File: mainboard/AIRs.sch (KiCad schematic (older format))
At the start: 37 parts, among them J10 AIR+, J6 AIR-, K1 KT12-1A, Q3 DMN10H220L, Q5 2N7002NXAKR, Q6 2N7002NXAKR, Q7 DMN10H220L, U11 TS3704IPT

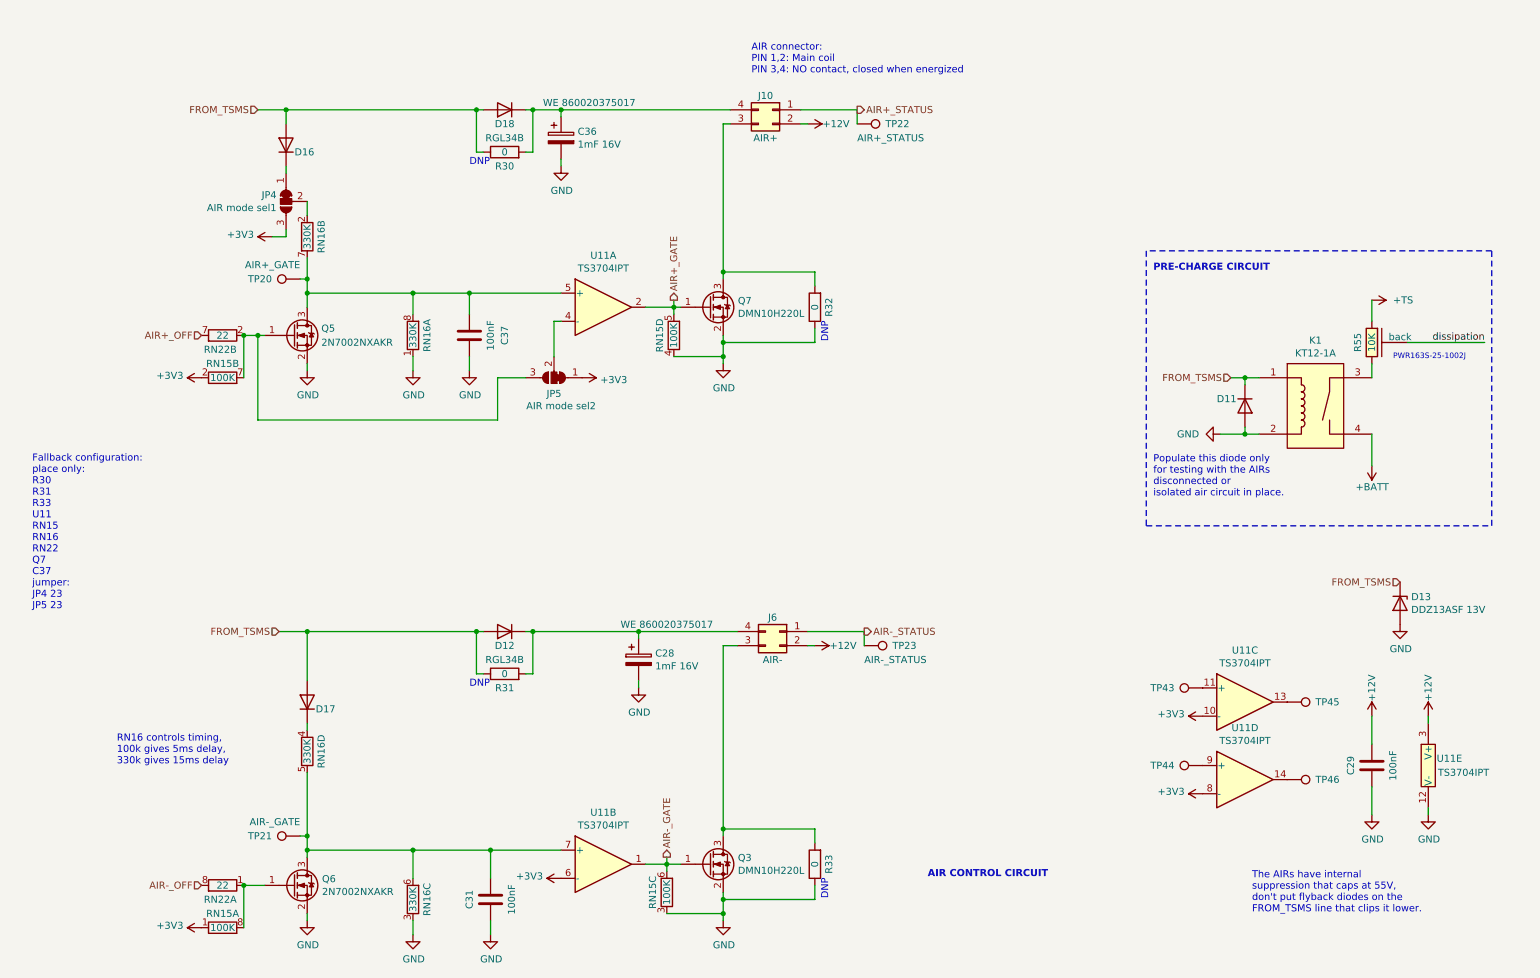
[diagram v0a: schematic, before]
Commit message: Renamed handcart detection
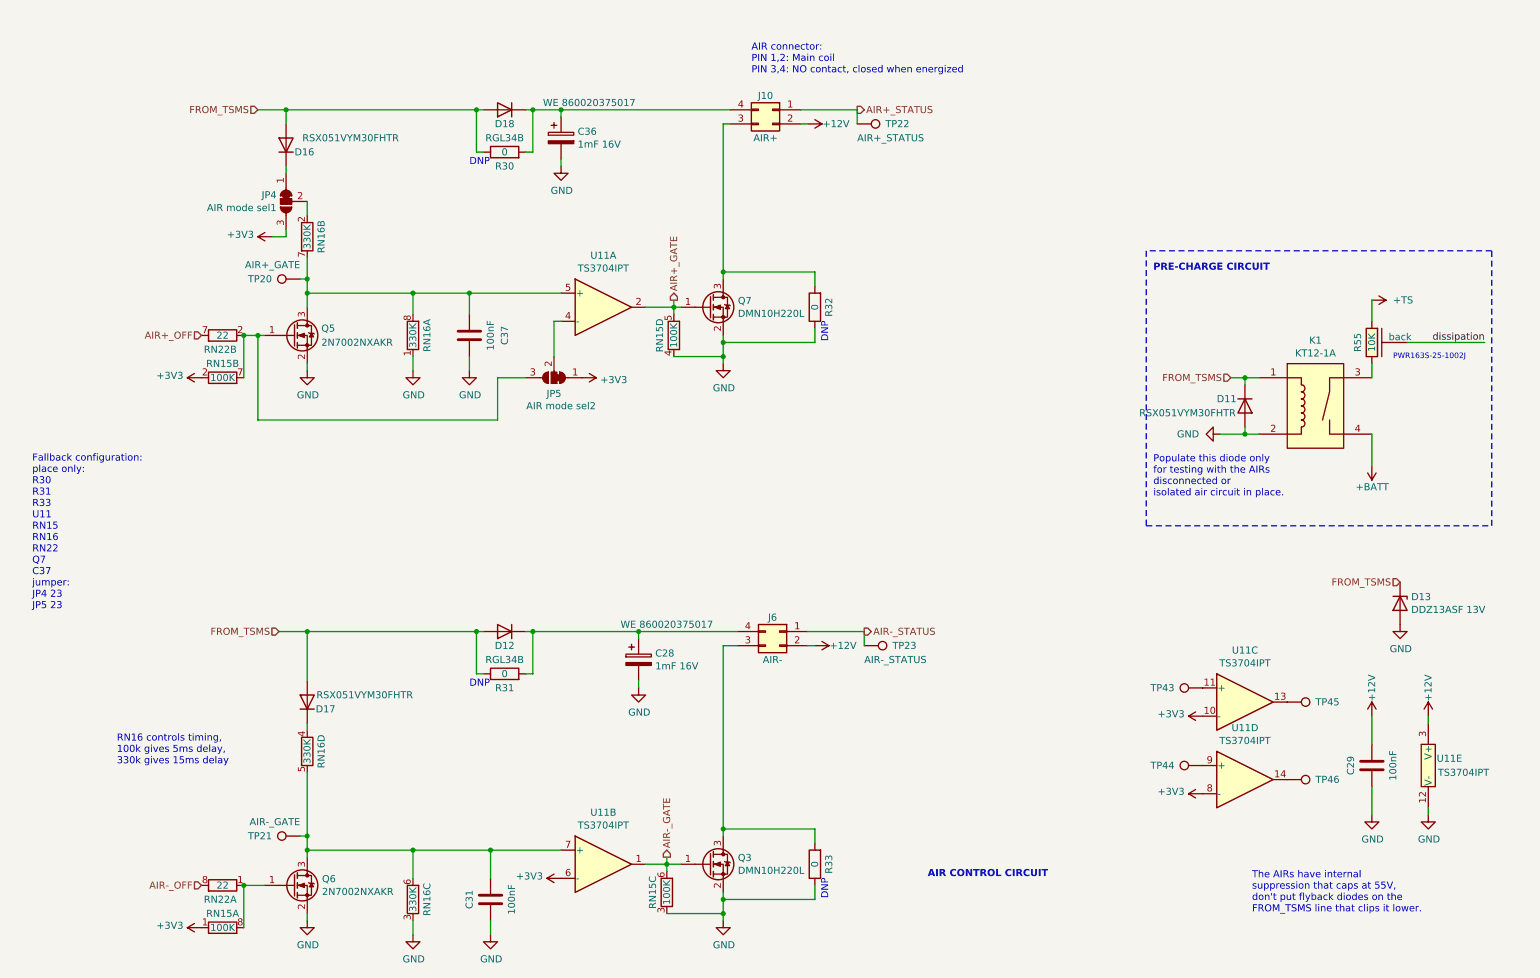
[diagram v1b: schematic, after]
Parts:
- D11, D16, D17: value D -> RSX051VYM30FHTR
- Q5, Q6: value 2N7002NXAKR -> 2N7002NXAKR
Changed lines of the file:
@@
 AR Path="/60A98674/60AA9B96" Ref="D16"  Part="1"
 F 0 "D16" V 2400 1250 50  0000 L CNN
-F 1 "D" V 2500 1250 50  0001 L CNN
+F 1 "RSX051VYM30FHTR" V 2500 650 50  0000 L CNN
 F 2 "MainBoard:SOD_323HE" H 2450 1450 50  0001 C CNN
 F 3 "~" H 2450 1450 50  0001 C CNN
@@
 AR Path="/60A98674/60AA9BEA" Ref="D17"  Part="1"
 F 0 "D17" V 2550 5200 50  0000 L CNN
-F 1 "D" V 2650 5200 50  0001 L CNN
+F 1 "RSX051VYM30FHTR" V 2650 4650 50  0000 L CNN
 F 2 "MainBoard:SOD_323HE" H 2600 5400 50  0001 C CNN
 F 3 "~" H 2600 5400 50  0001 C CNN
@@
 AR Path="/60A98674/60AA9C51" Ref="Q5"  Part="1"
 F 0 "Q5" H 2700 2850 50  0000 L CNN
-F 1 "2N7002NXAKR " H 2700 2750 50  0000 L CNN
+F 1 "2N7002NXAKR" H 2700 2750 50  0000 L CNN
 F 2 "Package_TO_SOT_SMD:SOT-23" H 2700 2725 50  0001 L CIN
 F 3 "https://www.onsemi.com/pub/Collateral/NDS7002A-D.PDF" H 2500 2800 50  0001 L CNN
@@
 AR Path="/60A98674/60FEED0A" Ref="D11"  Part="1"
 F 0 "D11" V 9200 3100 50  0000 L CNN
-F 1 "D" V 9300 3100 50  0001 L CNN
+F 1 "RSX051VYM30FHTR" V 9300 2550 50  0000 L CNN
 F 2 "MainBoard:SOD_323HE" H 9250 3300 50  0001 C CNN
 F 3 "~" H 9250 3300 50  0001 C CNN
@@
 AR Path="/60A98674/60AA9C5A" Ref="Q6"  Part="1"
 F 0 "Q6" H 2705 6746 50  0000 L CNN
-F 1 "2N7002NXAKR " H 2705 6655 50  0000 L CNN
+F 1 "2N7002NXAKR" H 2705 6655 50  0000 L CNN
 F 2 "Package_TO_SOT_SMD:SOT-23" H 2700 6625 50  0001 L CIN
 F 3 "https://www.onsemi.com/pub/Collateral/NDS7002A-D.PDF" H 2500 6700 50  0001 L CNN

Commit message: Correction almost finished, Started layouting
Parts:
- removed D11, D16, D17: RSX051VYM30FHTR, MainBoard:SOD_323HE, symbol Device:D
- removed R30, R31, R32, R33: 0, Resistor_SMD:R_0603_1608Metric, symbol Device:R
- removed TP43: 11, TestPoint:TestPoint_Pad_D1.0mm, symbol Connector:TestPoint
- removed TP44: 9, TestPoint:TestPoint_Pad_D1.0mm, symbol Connector:TestPoint
- removed TP45: 13, TestPoint:TestPoint_Pad_D1.0mm, symbol Connector:TestPoint
- removed TP46: 14, TestPoint:TestPoint_Pad_D1.0mm, symbol Connector:TestPoint
- removed U11: TS3704IPT, Package_SO:TSSOP-14_4.4x5mm_P0.65mm, symbol MainBoard:TS3704
- added D11, D16, D17: 1N4148W, Diode_SMD:D_SOD-123, symbol Diode:1N4148W
- added D19: DDZ13ASF 13V, Diode_SMD:D_SOD-323, symbol Device:D_Zener
- added JP7, JP8: SolderJumper_2_Open, Jumper:SolderJumper-2_P1.3mm_Open_RoundedPad1.0x1.5mm, symbol Jumper:SolderJumper_2_Open
- added Q16: 2N7002NXAKR, Package_TO_SOT_SMD:SOT-23, symbol Transistor_FET:2N7002
- added RN25: 22, Resistor_SMD:R_Array_Convex_4x0603, symbol Device:R_Pack04_Split
- added U4: TS3702IPT, Package_SO:TSSOP-8_4.4x3mm_P0.65mm, symbol Eagle_Main:TS3702
- D12, D18: symbol MainBoard:RGL34x -> Eagle_Main:RGL34x
- J10, J6: footprint MainBoard:Molex_Micro-Fit_3.0_43045-0412_2x02_P3.00mm_Vertical -> Connector_Molex:Molex_Micro-Fit_3.0_43045-0412_2x02_P3.00mm_Vertical; symbol Connector_Generic:Conn_02x02_Counter_Clockwise -> Connector_Generic:Conn_02x02_Top_Bottom
- K1: footprint MainBoard:KT_THT -> Eagle_Main:KT12_THT; symbol MainBoard:KT12-1A -> Eagle_Main:KT12-1A
- Q3, Q7: value DMN10H220L -> DMN10H220LK3; footprint Package_TO_SOT_SMD:SOT-23 -> Package_TO_SOT_SMD:TO-252-2; symbol Transistor_FET:DMN10H220L -> Device:Q_NMOS_GDS
- R55: footprint MainBoard:pwr163 -> Eagle_Main:PWR163; symbol MainBoard:R_power_backplane -> Eagle_Main:R_heatsink; Partname (none) -> PWR163S-25-1002J
- RN15, RN16, RN22: footprint MainBoard:R_network_4x1_bourns_CAY16 -> Resistor_SMD:R_Array_Convex_4x0603
- TP20: value AIR+_GATE -> AIR+_DELAY
- TP21: value AIR-_GATE -> AIR-_DELAY
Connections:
- net +12V: now also U4.8 (V+)
- net +3V3: now also U4.6 (_)
- net AIR+_GATE: now also RN25.4 (R4.1)
- net AIR-_GATE: now also RN25.2 (R2.1)
- net GND: now also Q3.3 (S), Q7.3 (S), RN16.2 (R2.1), D19.2 (A), JP7.2 (B), JP8.2 (B), Q16.2 (S), U4.4 (V-); no longer K1.2, Q3.2 (S), Q7.2 (S), RN16.1 (R1.1)
- net at JP4.1 (A): now also D16.1 (K)
- net at C37.1, Q5.3 (D), RN16.7 (R2.2)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: now also RN16.1 (R1.1), U4.3 (+); no longer RN16.8 (R1.2)
- net at J10.3 (Pin_3): now also Q7.2 (D), JP7.1 (A); no longer Q7.3 (D)
- net at RN16.4 (R4.1): now also D17.1 (K)
- net at JP4.2 (C): now also RN16.8 (R1.2); no longer RN16.2 (R2.1)
- net at C31.1, Q6.3 (D), RN16.5 (R4.2)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: now also U4.5 (+)
- net at J6.3 (Pin_3): now also Q3.2 (D), JP8.1 (A); no longer Q3.3 (D)
- net at JP5.2 (C): now also U4.2 (-)
- net PRECHARGE_HV_SENSE: now reaches K1.3, R55.1
- net FROM_TSMS renamed SD_END
- net SD_END: now also D11.1 (K), D16.2 (A), D17.2 (A)
- net dissipation: no longer names the net of R55.3 (HS)
- new net: RN25.5 (R4.2), U4.1
- new net: RN25.7 (R2.2), U4.7
- new net: Q16.1 (G), RN25.1 (R1.1)
- new net PRECHARGE: RN25.8 (R1.2)
- new net PRECHARGE_D: D11.2 (A), D19.1 (K), K1.2, Q16.3 (D)
- no-connect marks 0 -> 3
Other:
- note added: "AIR: GV240BAB\nAIR connector:\nPIN 3,4: Main coil\nPIN 1,2: Aux NC contact, open when energized\nAIRx_STATUS: \nH safe,AIR open\nL unsafe, AIR closed\n"
- note removed: "AIR CONTROL CIRCUIT\n"
- note removed: "AIR connector:\nPIN 1,2: Main coil\nPIN 3,4: NO contact, closed when energized"
- note removed: "DNP"
- note removed: "PWR163S-25-1002J"
- note removed: "Populate this diode only\nfor testing with the AIRs \ndisconnected or \nisolated air circuit in place."
- note removed: "The AIRs have internal \nsuppression that caps at 55V, \ndon't put flyback diodes on the \nFROM_TSMS line that clips it lower."
- moved on the sheet: C28, C31, C36, C37, D12, D13, D18, J10, J6, JP4, JP5, K1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
